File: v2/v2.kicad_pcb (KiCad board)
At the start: 2 copper layers, 170.5 x 144.8 mm, 112 parts, among them J2 Conn_01x04_Pin, J3 Conn_01x04_Pin, SW1 SW_Push, SW10 SW_Push, SW11 SW_Push, SW12 SW_Push, SW13 SW_Push, SW14 SW_Push, SW15 SW_Push, SW16 SW_Push, SW17 SW_Push, SW18 SW_Push, SW19 SW_Push, SW2 SW_Push, SW20 SW_Push, SW21 SW_Push, SW22 SW_Push, SW23 SW_Push, SW24 SW_Push, SW25 SW_Push, SW26 SW_Push, SW27 SW_Push, SW28 SW_Push, SW29 SW_Push, SW3 SW_Push, SW30 SW_Push, SW31 SW_Push, SW32 SW_Push, SW33 RotaryEncoder_Switch, SW4 SW_Push, SW5 SW_Push, SW6 SW_Push, SW7 SW_Push, SW8 SW_Push, SW9 SW_Push, U1 Pico, U2 Pico

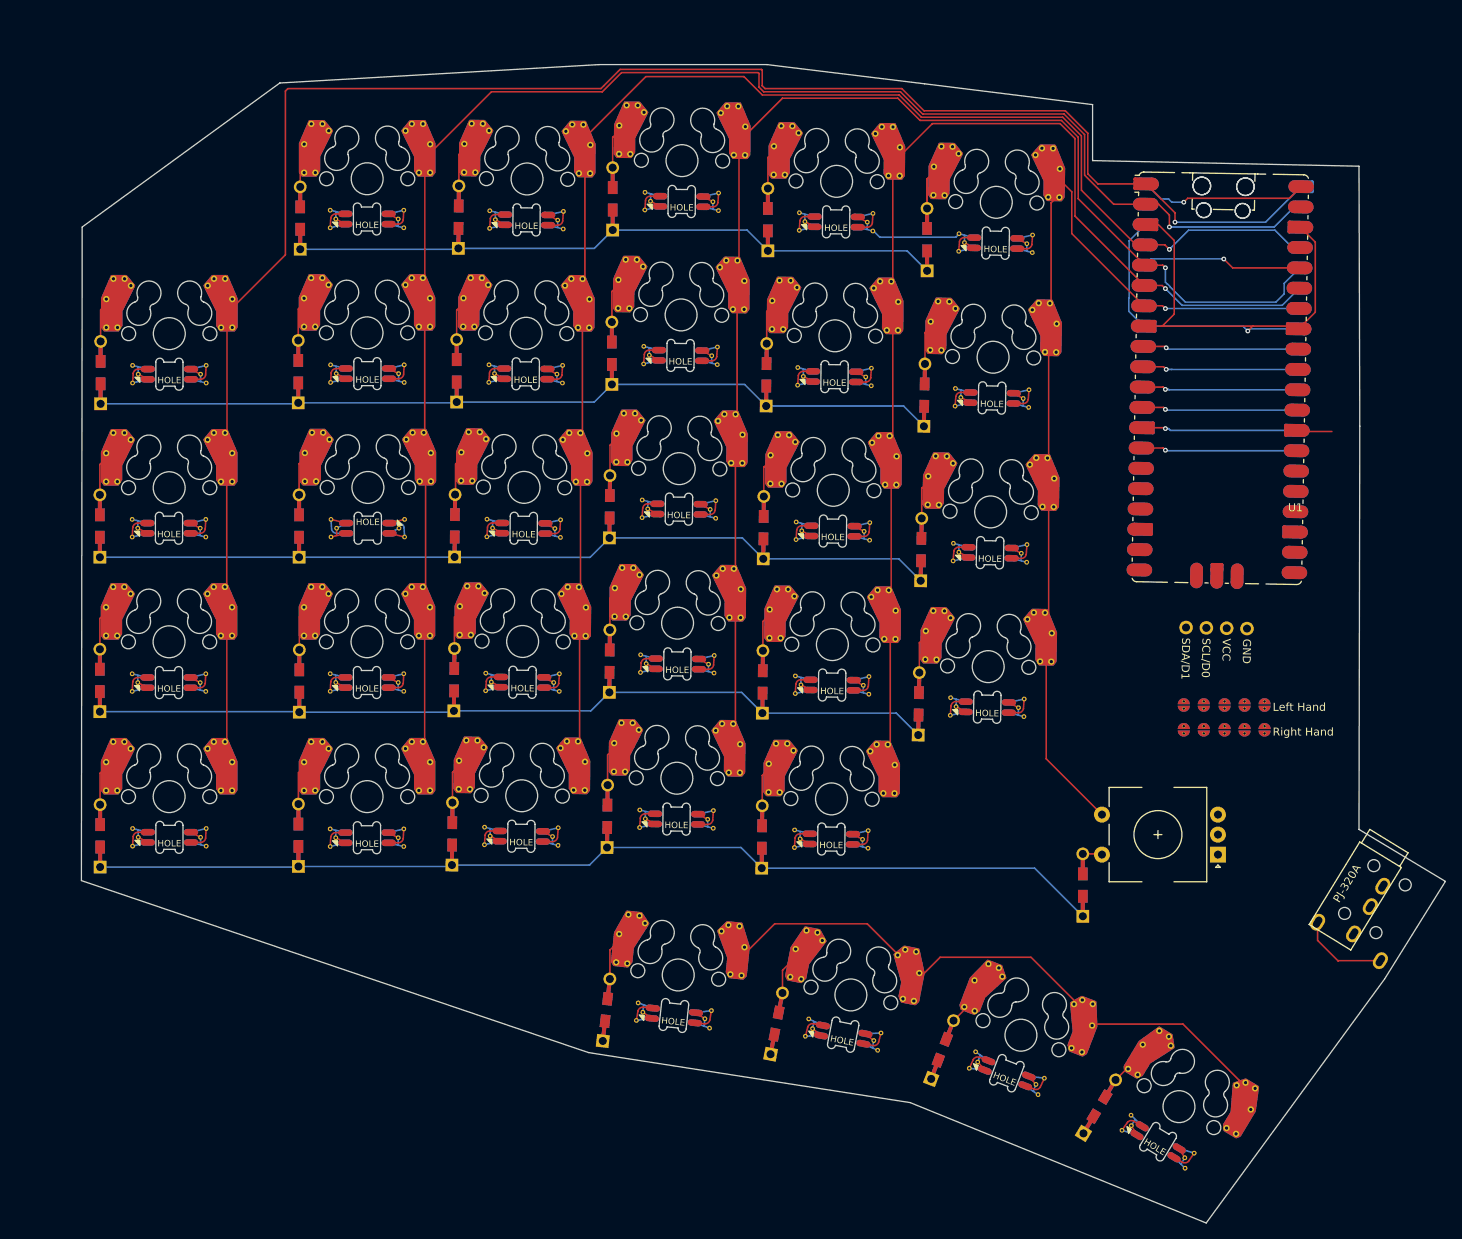
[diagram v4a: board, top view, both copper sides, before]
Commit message: finished routing and make fill zones
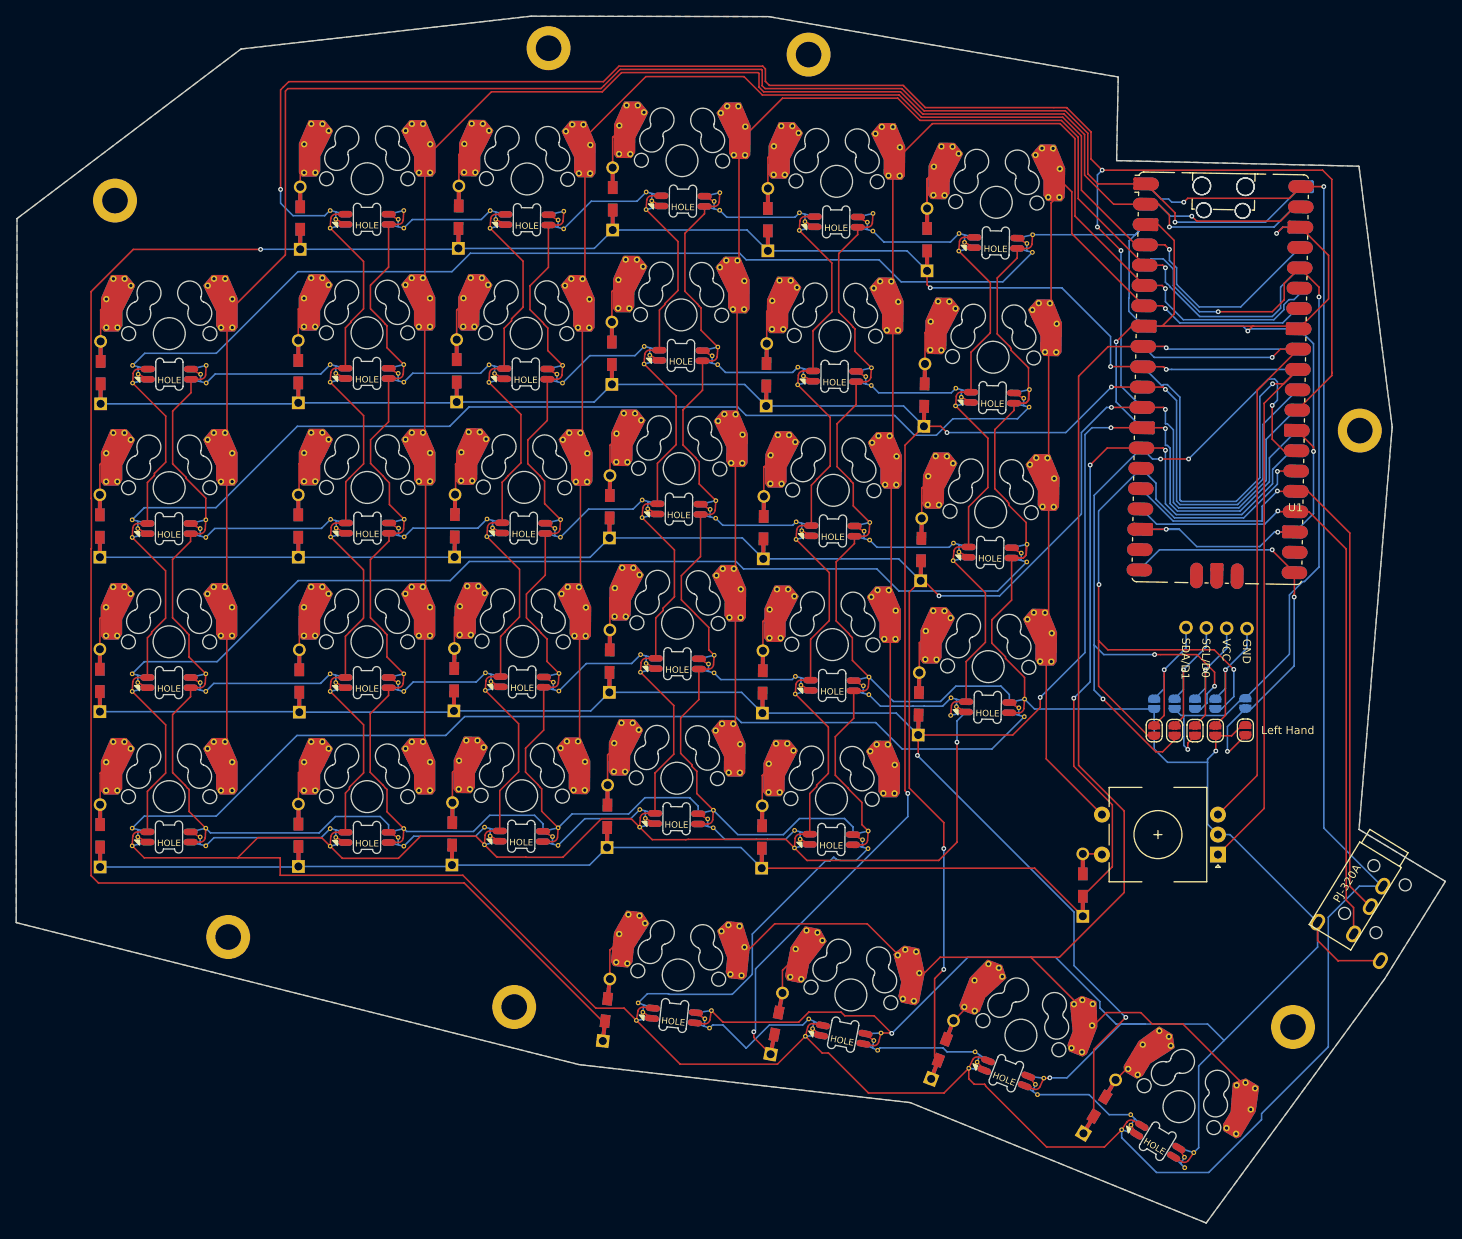
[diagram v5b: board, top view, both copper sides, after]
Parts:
- added REF**: MountingHole_3.2mm_M3_ISO14580_Pad, Keebio-Parts:MountingHole_3.2mm_M3_ISO14580_Pad, F.Cu at (206.2, 81.5)
- added REF**: MountingHole_3.2mm_M3_ISO14580_Pad, Keebio-Parts:MountingHole_3.2mm_M3_ISO14580_Pad, F.Cu at (275.1, 128.6)
- added REF**: MountingHole_3.2mm_M3_ISO14580_Pad, Keebio-Parts:MountingHole_3.2mm_M3_ISO14580_Pad, F.Cu at (169.4, 200.6)
- added REF**: MountingHole_3.2mm_M3_ISO14580_Pad, Keebio-Parts:MountingHole_3.2mm_M3_ISO14580_Pad, F.Cu at (133.7, 191.8)
- added REF**: MountingHole_3.2mm_M3_ISO14580_Pad, Keebio-Parts:MountingHole_3.2mm_M3_ISO14580_Pad, F.Cu at (173.7, 80.8)
- added REF**: MountingHole_3.2mm_M3_ISO14580_Pad, Keebio-Parts:MountingHole_3.2mm_M3_ISO14580_Pad, F.Cu at (119.5, 99.8)
- added REF**: MountingHole_3.2mm_M3_ISO14580_Pad, Keebio-Parts:MountingHole_3.2mm_M3_ISO14580_Pad, F.Cu at (266.8, 203.1)
- JP1, JP2, JP4, JP5, JP7, JP8, JP9: footprint Keebio-Parts:solder_jumper -> Jumper:SolderJumper-2_P1.3mm_Open_RoundedPad1.0x1.5mm
- JP10, JP6: footprint Keebio-Parts:solder_jumper -> Jumper:SolderJumper-2_P1.3mm_Open_RoundedPad1.0x1.5mm; moved to B.Cu
- JP3: footprint Keebio-Parts:solder_jumper -> Jumper:SolderJumper-2_P1.3mm_Open_RoundedPad1.0x1.5mm; moved to F.Cu
- LED13: moved to F.Cu
- moved JP8 11.3 mm to (249.4, 162.7), turned to -90 degrees
- moved JP4 11.3 mm to (249.4, 166.1), turned to -90 degrees
- moved JP7 6.25 mm to (251.9, 162.7), turned to -90 degrees
- moved JP6 4.92 mm to (254.5, 162.7), turned to -90 degrees
- moved JP3 4.85 mm to (251.9, 166.1), turned to -90 degrees
- moved JP10 4.08 mm to (260.8, 162.7), turned to 90 degrees
- moved JP9 3.96 mm to (260.8, 166.0)
- moved JP5 3.95 mm to (257.1, 162.7), turned to -90 degrees
- moved JP1 3.95 mm to (257.1, 166.1)
- moved JP2 1.10 mm to (254.5, 166.1), turned to -90 degrees
- moved LED3 0.16 mm to (190.5, 94.8)
- moved SW16 0.10 mm to (151.0, 135.7)
- moved D16 0.10 mm to (142.4, 140.5)
- moved LED32 0.08 mm to (252.5, 213.0)
- moved LED31 0.07 mm to (232.7, 204.1)
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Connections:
- LED11 pad 1: Net-(LED10-DIN) -> Net-(LED11-DOUT)
- LED11 pad 3: Net-(LED11-DIN) -> Net-(LED10-DOUT)
- LED12 pad 1: Net-(LED11-DIN) -> Net-(LED12-DOUT)
- LED12 pad 3: Net-(LED12-DIN) -> Net-(LED11-DOUT)
- LED13 pad 1: Net-(LED12-DIN) -> Net-(LED13-DOUT)
- LED13 pad 3: Net-(LED13-DIN) -> Net-(LED12-DOUT)
- LED14 pad 1: Net-(LED13-DIN) -> Net-(LED14-DOUT)
- LED14 pad 3: Net-(LED14-DIN) -> Net-(LED13-DOUT)
- LED15 pad 3: Net-(LED15-DIN) -> Net-(LED14-DOUT)
- LED22 pad 3: Net-(LED22-DIN) -> Net-(LED21-DOUT)
- LED23 pad 1: Net-(LED22-DIN) -> Net-(LED23-DOUT)
- LED23 pad 3: Net-(LED23-DIN) -> Net-(LED22-DOUT)
- LED24 pad 1: Net-(LED23-DIN) -> Net-(LED24-DOUT)
- LED24 pad 3: Net-(LED24-DIN) -> Net-(LED23-DOUT)
- LED25 pad 1: Net-(LED24-DIN) -> Net-(LED25-DOUT)
- LED25 pad 3: Net-(LED25-DIN) -> Net-(LED24-DOUT)
- LED26 pad 1: Net-(LED25-DIN) -> Net-(LED26-DOUT)
- LED26 pad 3: Net-(LED26-DIN) -> Net-(LED25-DOUT)
- LED27 pad 1: Net-(LED26-DIN) -> Net-(LED27-DOUT)
- LED27 pad 3: Net-(LED27-DIN) -> Net-(LED26-DOUT)
- LED28 pad 1: Net-(LED27-DIN) -> Net-(LED28-DOUT)
- LED28 pad 3: Net-(LED21-DOUT) -> Net-(LED27-DOUT)
- LED29 pad 1: unconnected-(LED29-DOUT-Pad1) -> Net-(LED29-DOUT)
- LED29 pad 3: Net-(LED22-DOUT) -> Net-(LED28-DOUT)
- LED30 pad 3: unconnected-(LED30-DIN-Pad3) -> Net-(LED29-DOUT)
- LED7 pad 1: Net-(LED14-DIN) -> Net-(LED7-DOUT)
- LED8 pad 1: Net-(LED15-DIN) -> Net-(LED8-DOUT)
- LED8 pad 3: Net-(LED8-DIN) -> Net-(LED7-DOUT)
- LED9 pad 1: Net-(LED8-DIN) -> Net-(LED10-DIN)
- LED9 pad 3: Net-(LED10-DOUT) -> Net-(LED8-DOUT)
- SW33 pad A: ENC A -> ENC B
- SW33 pad B: ENC B -> ENC A
- U1 pad 29: unconnected-(U1-GPIO22-Pad29) -> SK6912PWM
- U2 pad 29: unconnected-(U2-GPIO22-Pad29) -> SK6912PWM
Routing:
- net VBUS: track 21.1 -> 883.7 mm, vias 1 -> 3
- net GND: track 100.2 -> 943.5 mm, vias 1 -> 9
- net SK6912PWM: track 0.00 -> 225.6 mm, vias 0 -> 4
- net Row 1: track 101.0 -> 309.3 mm, vias 1 -> 4
- net Row 2: track 125.6 -> 267.3 mm, vias 1 -> 5
- net Row 4: track 125.1 -> 261.2 mm, vias 1 -> 5
- net Row 3: track 125.3 -> 252.0 mm, vias 1 -> 5
- net Net-(LED5-DOUT): track 0.00 -> 121.3 mm
- net Net-(LED11-DOUT): track 0.00 -> 120.9 mm
- net Net-(LED17-DOUT): track 0.00 -> 120.7 mm
- net Net-(LED23-DOUT): track 0.00 -> 120.6 mm
- net ENC B: track 0.00 -> 111.6 mm, vias 0 -> 1
- net SDL: track 0.00 -> 102.5 mm, vias 0 -> 6
- net Col 7: track 104.7 -> 197.5 mm
- net SDA: track 0.00 -> 90.2 mm, vias 0 -> 3
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- added copper zone on B.Cu, net GND
- added copper zone on F.Cu, net GND
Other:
- board size 170.5 x 144.8 mm -> 178.7 x 150.8 mm
